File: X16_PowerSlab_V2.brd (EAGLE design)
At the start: 152.4 x 76.2 mm, 42 parts, among them J1 CONN_796636-3, J2 CONN_796636-3, J3 CONN_ET60T

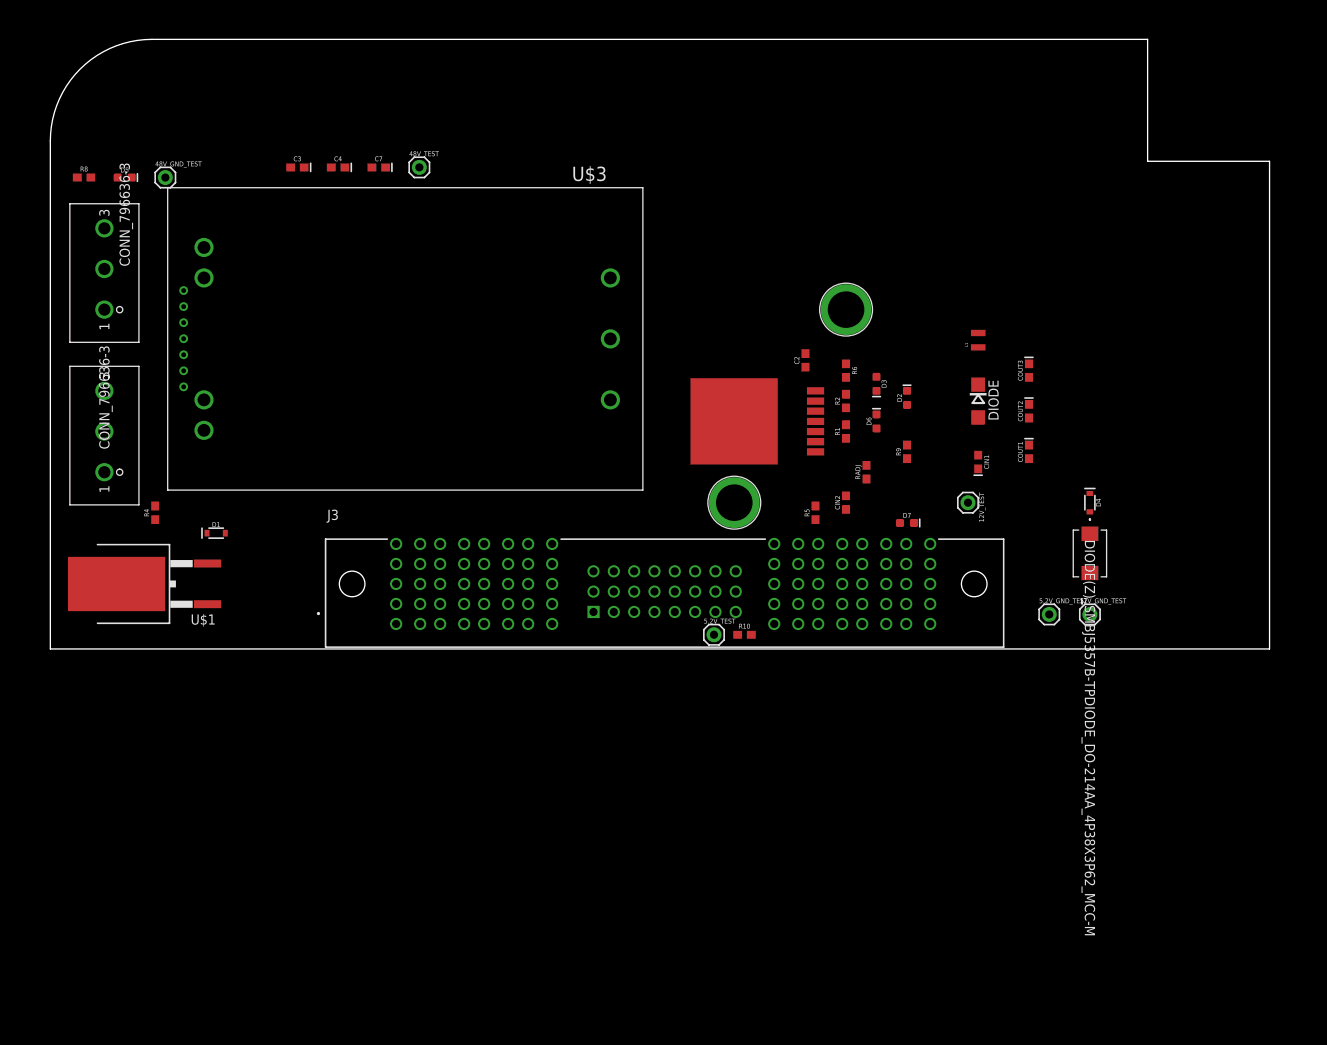
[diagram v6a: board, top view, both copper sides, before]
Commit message: set up polygons
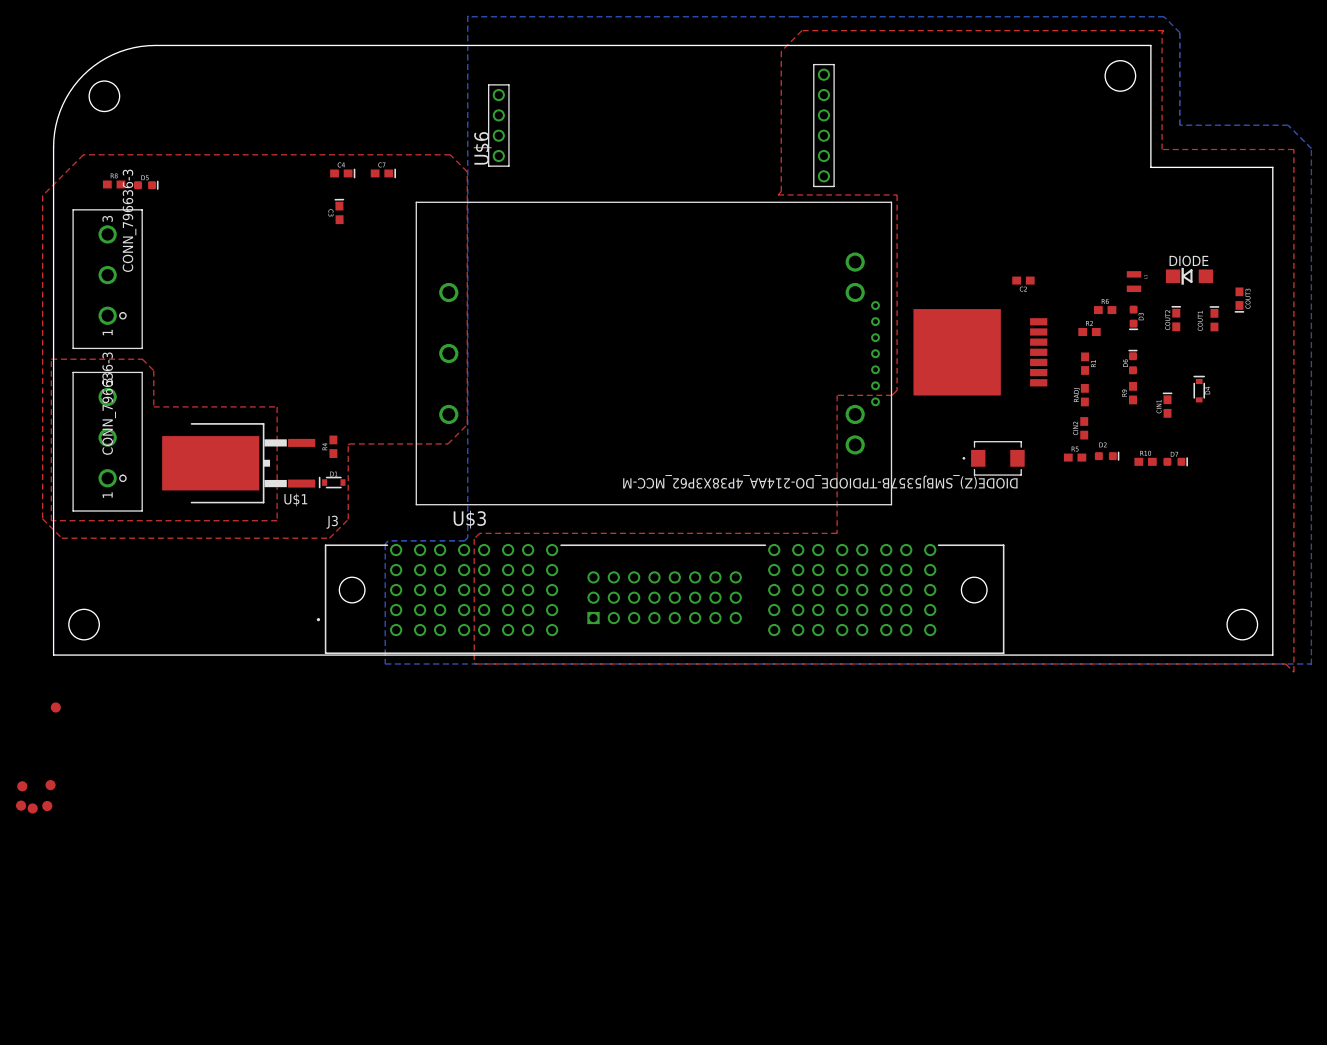
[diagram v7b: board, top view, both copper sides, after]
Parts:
- removed 12V_GND_TEST, 12V_TEST, 48V_GND_TEST, 48V_TEST, 5.2V_GND_TEST, 5.2V_TEST: (no value), SparkFun-Connectors:1X01
- removed U$4: 5.2V_TESTPOINT, X15-Conversion-Parts-Library:5.2V_TESTPOINT
- removed U$5: 12V_TESTPOINT, X15-Conversion-Parts-Library:12V_TESTPOINT
- added 12VGND_TP, 12V_TP, 48VGND_TP, 48_TP, TP5, TP6: TEST-POINT3X5, SparkFun-Connectors:PAD.03X.05
- added H1, H2, H3, H4: 6-32-HOLE, X15_Brickstribution:6-32-HOLE
- added U$6: CONN_DISTRIBUTION_TO_CONVERSION, X16_Power_Slab:TSW-105-05-G-S(D-C)
- moved R10 54.6 mm to (136.5, 24.2)
- moved U$3 48.7 mm to (45.3, 18.8), turned to 0 degrees
- moved D7 34.3 mm to (140.1, 24.2)
- moved R6 33.3 mm to (131.4, 43.1), turned to 0 degrees
- moved D3 33.2 mm to (135.0, 42.3)
- moved R5 33.2 mm to (127.7, 24.7), turned to 0 degrees
- moved D6 32.9 mm to (134.9, 36.5)
- moved R2 31.6 mm to (129.5, 40.4), turned to 0 degrees
- moved CIN2 31.2 mm to (128.8, 28.3)
- moved R1 31.1 mm to (128.9, 36.4), turned to 270 degrees
- moved DIODE 30.7 mm to (142.0, 47.3), turned to 0 degrees
- moved U$2 29.2 mm to (123.1, 41.7)
- moved R9 29.2 mm to (134.9, 32.7)
- moved C2 29.0 mm to (121.2, 46.8), turned to 180 degrees
- moved RADJ 29.0 mm to (128.9, 32.5)
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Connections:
- removed net 12V_GND: J3.P03_1, J3.P03_10, J3.P03_2, J3.P03_3, J3.P03_4, J3.P03_5, J3.P03_6, J3.P03_7, J3.P03_8, J3.P03_9, J3.P04_1, J3.P04_10, J3.P04_2, J3.P04_3, J3.P04_4, J3.P04_5, J3.P04_6, J3.P04_7, J3.P04_8, J3.P04_9
- new net 5V: U$6.7, U$6.8
- net 12V: now also U$6.1, U$6.2, U$6.3, U$6.4; no longer 12V_TEST.1, U$5.12V
- net 48V: no longer 48V_TEST.1
- net 48V_GND: no longer 48V_GND_TEST.1
- net 5.2V: no longer 5.2V_TEST.1, U$4.5.2V
- net GND: now also J3.P03_1, J3.P03_10, J3.P03_2, J3.P03_3, J3.P03_4, J3.P03_5, J3.P03_6, J3.P03_7, J3.P03_8, J3.P03_9, J3.P04_1, J3.P04_10, J3.P04_2, J3.P04_3, J3.P04_4, J3.P04_5, J3.P04_6, J3.P04_7, J3.P04_8, J3.P04_9, U$6.10, U$6.9; no longer 12V_GND_TEST.1, 5.2V_GND_TEST.1
- net PMBUS_CTRL: now also J3.23; no longer J3.17
- net PMBUS_GND: now also J3.22; no longer J3.18
- net PMBUS_SA0: now also J3.17; no longer J3.22
- net PMBUS_SA1: now also J3.18; no longer J3.23
- net PMBUS_SCL: now also J3.19; no longer J3.21
- net PMBUS_SDA: now also J3.21; no longer J3.19
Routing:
- added copper zone on layer 16, net 12V
- added copper zone on layer 1, net 48V_GND
- added copper zone on layer 1, net GND
- added copper zone on layer 1, net GND_RAW

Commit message: worked on routing
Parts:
- moved C3 23.2 mm to (12.8, 51.7), turned to 90.1 degrees
- moved R8 17.2 mm to (13.2, 42.6)
- moved D5 16.1 mm to (16.3, 43.4), turned to 90 degrees
- moved 12VGND_TP 11.5 mm to (0.69, -18.0)
- moved 48VGND_TP 6.38 mm to (0.03, -13.9)
- moved 12V_TP 5.34 mm to (2.06, -14.4)
- moved TP5 4.93 mm to (1.98, -17.4)
- moved TP6 3.37 mm to (-0.69, -17.4)
- moved 48_TP 1.15 mm to (-1.52, -16.4)
- moved D7 0.61 mm to (140.6, 23.8)
- moved C2 0.54 mm to (121.6, 46.5), turned to 0 degrees
- moved R10 0.39 mm to (136.3, 23.8), turned to 359.6 degrees
- moved D2 0.20 mm to (131.5, 24.7)
- moved C4 0.18 mm to (36.1, 60.3)
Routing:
- net 48V: track 0.00 -> 97.2 mm
- net 5.2V: track 0.00 -> 82.5 mm
- net 12V: track 0.00 -> 82.2 mm, vias 0 -> 1
- net PMBUS_SA0: track 0.00 -> 49.3 mm
- net PMBUS_SA1: track 0.00 -> 46.0 mm
- net PMBUS_SCL: track 0.00 -> 42.6 mm
- net PMBUS_SALERT: track 0.00 -> 39.4 mm
- net N$2: track 0.00 -> 36.4 mm, vias 0 -> 1
- net PMBUS_SDA: track 0.00 -> 36.3 mm
- net PMBUS_GND: track 0.00 -> 33.9 mm
- net PMBUS_CTRL: track 0.00 -> 30.5 mm
- net N$1: track 0.00 -> 11.3 mm
- net N$8: track 0.00 -> 10.5 mm
- net N$4: track 0.00 -> 8.83 mm
- net N$5: track 0.00 -> 2.71 mm
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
